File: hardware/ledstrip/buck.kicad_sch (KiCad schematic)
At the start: 5 parts, among them U3 TPS62162DSG

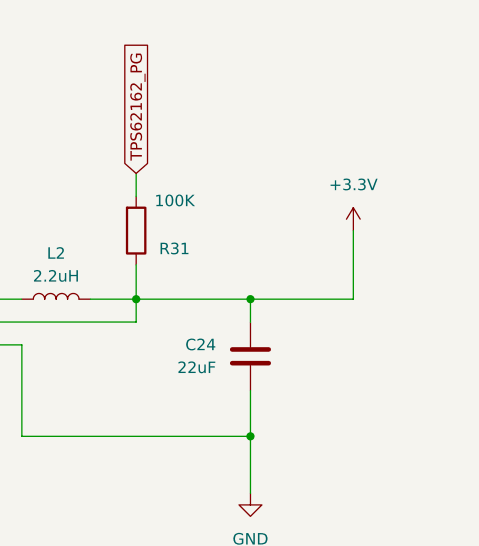
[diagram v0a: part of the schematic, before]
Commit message: Fix ERC errors.
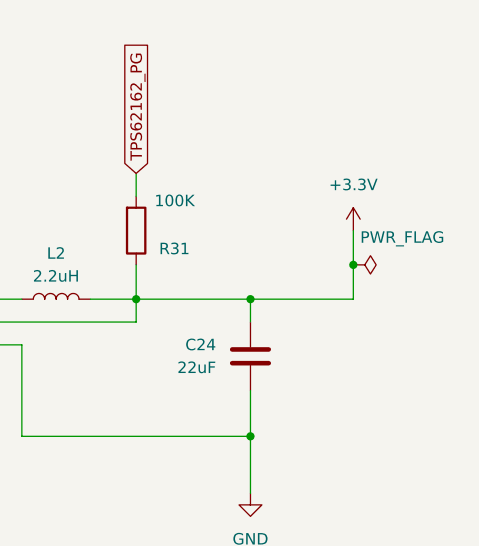
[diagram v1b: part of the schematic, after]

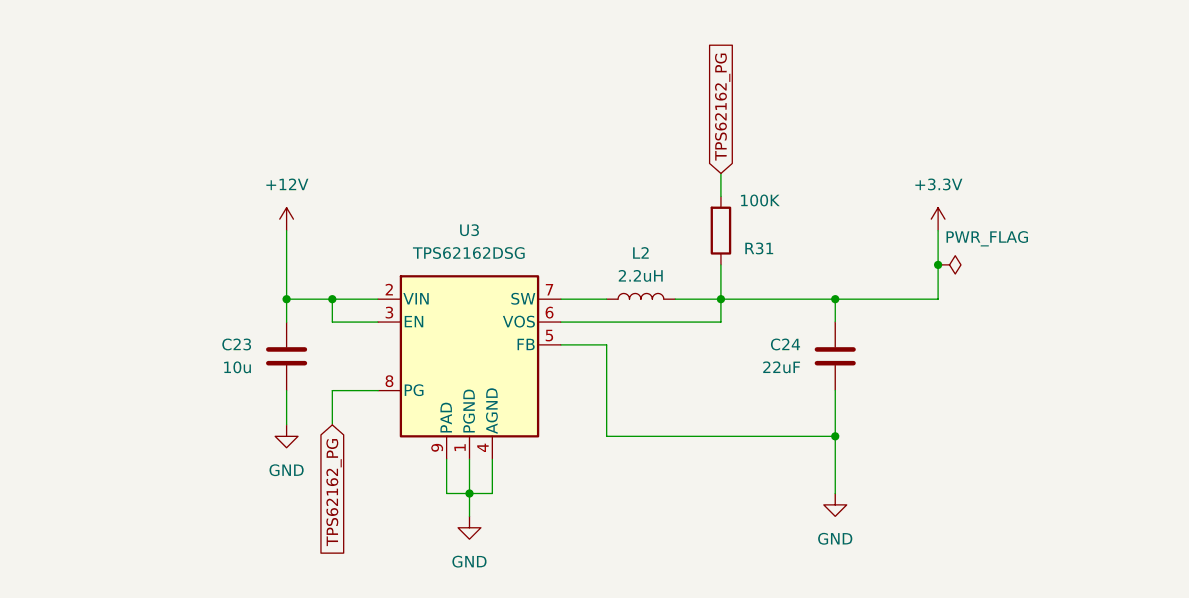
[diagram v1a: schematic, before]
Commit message: Fix last errors in schematics
Missing footprint, missing distributor link.
Updated project sym-lib-table for ERC checks.
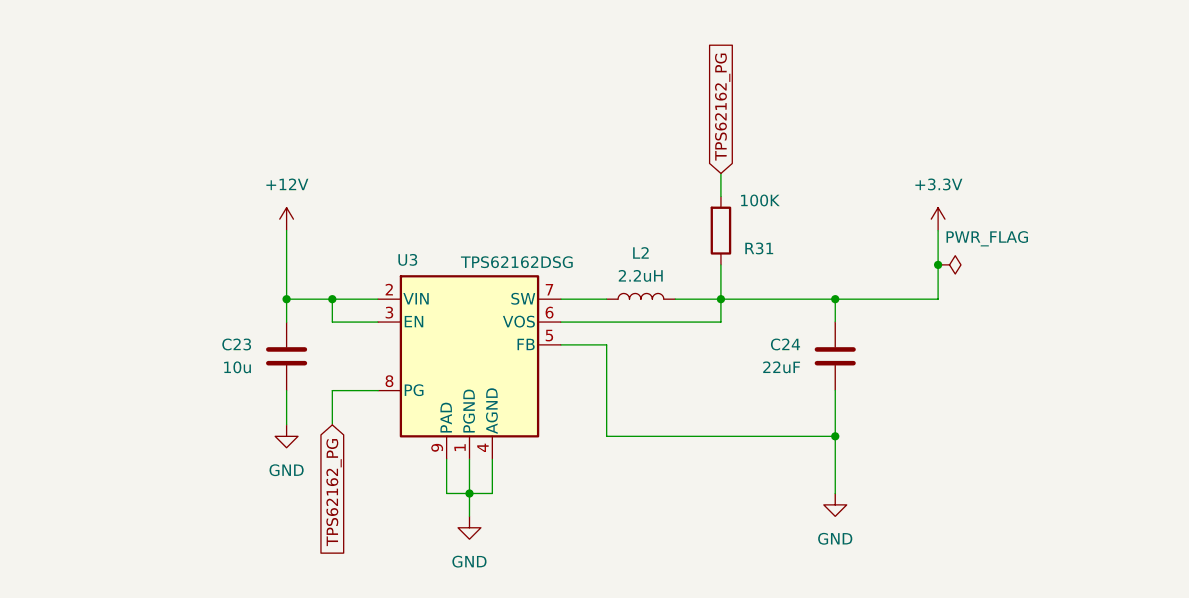
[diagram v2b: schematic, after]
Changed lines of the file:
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@@
 		(on_board yes)
 		(dnp no)
-		(fields_autoplaced yes)
 		(property "Reference" "U3"
-			(at 132.08 71.12 0)
+			(at 125.222 74.422 0)
 			(effects
 				(font
@@
 		)
 		(property "Value" "TPS62162DSG"
-			(at 132.08 73.66 0)
+			(at 137.414 74.676 0)
 			(effects
 				(font

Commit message: Add label on nodes.
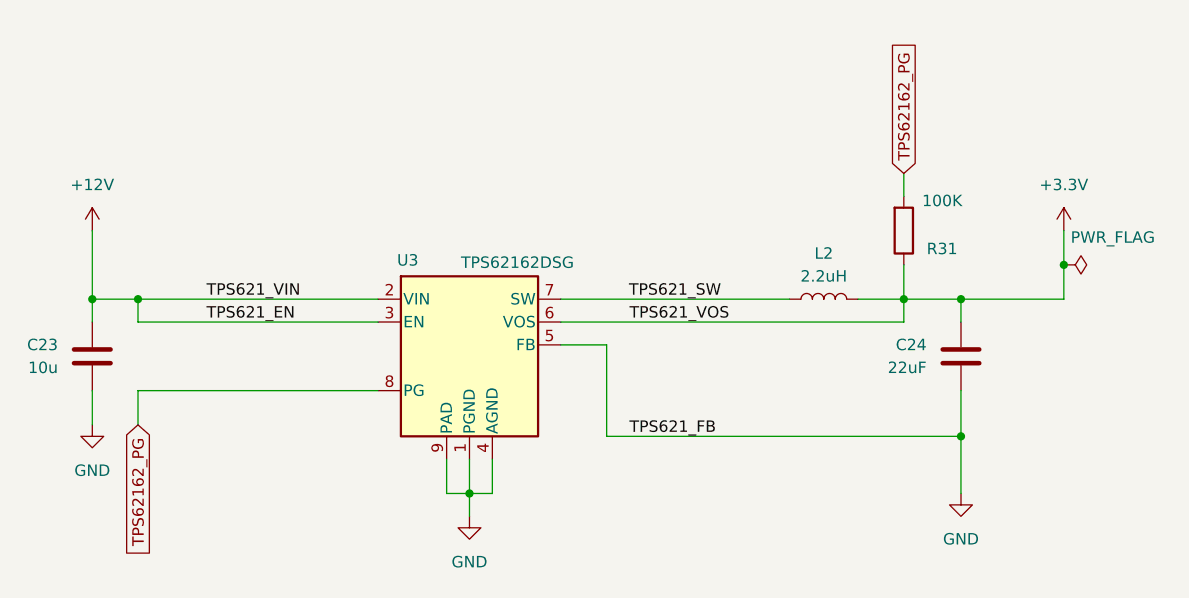
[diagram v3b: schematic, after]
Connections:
- net TPS621_SW: now reaches L2.1, U3.7 (SW)
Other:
- moved on the sheet: C23, C24, L2, R31

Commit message: Fix ERC warnings.
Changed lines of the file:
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@@
-		)
-	)
-	(label "TPS621_VIN"
-		(at 102.87 78.74 0)
-		(effects
-			(font
-				(size 1.27 1.27)
-			)
-			(justify left bottom)
-		)
-	)
-	(label "TPS621_VOS"
-		(at 149.86 81.28 0)
-		(effects
-			(font
-				(size 1.27 1.27)
-			)
-			(justify left bottom)
 		)
 	)
@@
 		(effects
 			(font
-				(size 1.27 1.27)
-			)
-			(justify left bottom)
-		)
-	)
-	(label "TPS621_FB"
-		(at 149.86 93.98 0)
-		(effects
-			(font
-				(size 1.27 1.27)
-			)
-			(justify left bottom)
-		)
-	)
-	(label "TPS621_EN"
-		(at 102.87 81.28 0)
-		(effects
-			(font

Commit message: Minor fixes
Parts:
- C23, C24: MPN (none) -> CL21A106KAYNNN; Manufacturer Part Number CL21A106KAYNNN -> (none)
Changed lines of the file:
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@@
 			)
 		)
-		(property "Manufacturer Part Number" "CL21A106KAYNNN"
+		(property "MPN" "CL21A106KAYNNN"
 			(at 186.69 85.09 0)
 			(effects
@@
 		)
 		(property "Distributor Link 2" "https://www.digikey.fr/fr/products/detail/samsung-electro-mechanics/CL10A226MQ8NRNC/3886851?srsltid=AfmBOopkT6AFjlXVjJGYlzyBS9Mt43m1P9-6SG41ry0KTU876ZZObNuC"
-			(at 186.69 85.09 0)
-			(effects
-				(font
-					(size 1.27 1.27)
-				)
-				(hide yes)
-			)
-		)
-		(property "Disributor Link 1" ""
-			(at 186.69 85.09 0)
-			(effects
-				(font
-					(size 1.27 1.27)
-				)
-				(hide yes)
-			)
-		)
-		(property "Ditributor Link 1" ""
 			(at 186.69 85.09 0)
 			(effects
@@
 			)
 		)
-		(property "Manufacturer Part Number" "CL21A106KAYNNN"
+		(property "MPN" "CL21A106KAYNNN"
 			(at 90.17 85.09 0)
 			(effects
@@
 			)
 		)
-		(property "Disributor Link 1" ""
-			(at 90.17 85.09 0)
-			(effects
-				(font
-					(size 1.27 1.27)
-				)
-				(hide yes)
-			)
-		)
-		(property "Ditributor Link 1" ""
-			(at 90.17 85.09 0)
-			(effects
-				(font
-					(size 1.27 1.27)
-				)
-				(hide yes)
-			)
-		)
 		(pin "1"
 		)
@@
 		)
 		(property "Distributor Link 1" "https://www.mouser.fr/ProductDetail/Texas-Instruments/TPS62162DSGT?qs=gXEV9p%2FxLgc%252BlgWUUl7N3w%3D%3D"
-			(at 132.08 86.36 0)
-			(effects
-				(font
-					(size 1.27 1.27)
-				)
-				(hide yes)
-			)
-		)
-		(property "Disributor Link 1" ""
-			(at 132.08 86.36 0)
-			(effects
-				(font
-					(size 1.27 1.27)
-				)
-				(hide yes)
-			)
-		)
-		(property "Ditributor Link 1" ""
 			(at 132.08 86.36 0)
 			(effects
@@
 			)
 		)
-		(property "Disributor Link 1" ""
-			(at 171.45 78.74 90)
-			(effects
-				(font
-					(size 1.27 1.27)
-				)
-				(hide yes)
-			)
-		)
-		(property "Ditributor Link 1" ""
-			(at 171.45 78.74 90)
-			(effects
-				(font
-					(size 1.27 1.27)
-				)
-				(hide yes)
-			)
-		)
 		(pin "1"
 		)
@@
 			(at 180.34 71.12 0)
 			(effects
-				(font
-					(size 1.27 1.27)
-				)
-				(hide yes)
-			)
-		)
-		(property "Disributor Link 1" ""
-			(at 180.34 71.12 0)
-			(effects
-				(font
-					(size 1.27 1.27)
-				)
-				(hide yes)
-			)
-		)
-		(property "Ditributor Link 1" ""
-			(at 180.34 71.12 0)
-			(effects

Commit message: Update schematics symbols fields for manufactrurer
Update BOM fields.
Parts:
- L2: MPN (none) -> PFL3215-222MEC; Manufacturer (none) -> Coilcraft
- R31: MPN (none) -> RT0805BRB07100KL; Manufacturer (none) -> YAGEO
- U3: MPN (none) -> TPS62162DSGT; Manufacturer (none) -> Texas Instruments
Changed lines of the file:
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@@
+			)
+		)
+		(property "Disributor Link 1" ""
+			(at 186.69 85.09 0)
+			(effects
+				(font
+					(size 1.27 1.27)
+				)
+				(hide yes)
+			)
+		)
+		(property "Ditributor Link 1" ""
+			(at 186.69 85.09 0)
+			(effects
+				(font
+					(size 1.27 1.27)
+				)
+				(hide yes)
+			)
+		)
+		(property "Manufacturer Part Number" ""
+			(at 186.69 85.09 0)
+			(effects
+				(font
+					(size 1.27 1.27)
+				)
+				(hide yes)
 			)
 		)
@@
 			)
 		)
+		(property "Disributor Link 1" ""
+			(at 90.17 85.09 0)
+			(effects
+				(font
+					(size 1.27 1.27)
+				)
+				(hide yes)
+			)
+		)
+		(property "Ditributor Link 1" ""
+			(at 90.17 85.09 0)
+			(effects
+				(font
+					(size 1.27 1.27)
+				)
+				(hide yes)
+			)
+		)
+		(property "Manufacturer Part Number" ""
+			(at 90.17 85.09 0)
+			(effects
+				(font
+					(size 1.27 1.27)
+				)
+				(hide yes)
+			)
+		)
 		(pin "1"
 		)
@@
 		)
 		(property "Distributor Link 1" "https://www.mouser.fr/ProductDetail/Texas-Instruments/TPS62162DSGT?qs=gXEV9p%2FxLgc%252BlgWUUl7N3w%3D%3D"
+			(at 132.08 86.36 0)
+			(effects
+				(font
+					(size 1.27 1.27)
+				)
+				(hide yes)
+			)
+		)
+		(property "Manufacturer" "Texas Instruments"
+			(at 132.08 86.36 0)
+			(effects
+				(font
+					(size 1.27 1.27)
+				)
+				(hide yes)
+			)
+		)
+		(property "MPN" "TPS62162DSGT"
+			(at 132.08 86.36 0)
+			(effects
+				(font
+					(size 1.27 1.27)
+				)
+				(hide yes)
+			)
+		)
+		(property "Disributor Link 1" ""
+			(at 132.08 86.36 0)
+			(effects
+				(font
+					(size 1.27 1.27)
+				)
+				(hide yes)
+			)
+		)
+		(property "Ditributor Link 1" ""
+			(at 132.08 86.36 0)
+			(effects
+				(font
+					(size 1.27 1.27)
+				)
+				(hide yes)
+			)
+		)
+		(property "Manufacturer Part Number" ""
 			(at 132.08 86.36 0)
 			(effects
@@
 			)
 		)
+		(property "Manufacturer" "Coilcraft"
+			(at 171.45 78.74 90)
+			(effects
+				(font
+					(size 1.27 1.27)
+				)
+				(hide yes)
+			)
+		)
+		(property "MPN" "PFL3215-222MEC"
+			(at 171.45 78.74 90)
+			(effects
+				(font
+					(size 1.27 1.27)
+				)
+				(hide yes)
+			)
+		)
 		(property "Distributor Link 2" "https://www.coilcraft.com/en-us/products/power/shielded-inductors/molded-inductor/pfl/pfl3215/pfl3215-222/?srsltid=AfmBOooloSXEMlP32bATBb0fG8MwtySnY4A9GXMUtQt98iXKMXBtuEx7"
+			(at 171.45 78.74 90)
+			(effects
+				(font
+					(size 1.27 1.27)
+				)
+				(hide yes)
+			)
+		)
+		(property "Disributor Link 1" ""
+			(at 171.45 78.74 90)
+			(effects
+				(font
+					(size 1.27 1.27)
+				)
+				(hide yes)
+			)
+		)
+		(property "Ditributor Link 1" ""
+			(at 171.45 78.74 90)
+			(effects
+				(font
+					(size 1.27 1.27)
+				)
+				(hide yes)
+			)
+		)
+		(property "Manufacturer Part Number" ""
 			(at 171.45 78.74 90)
 			(effects
@@
 			)
 		)
+		(property "Manufacturer" "YAGEO"
+			(at 180.34 71.12 0)
+			(effects
+				(font
+					(size 1.27 1.27)
+				)
+				(hide yes)
+			)
+		)
+		(property "MPN" "RT0805BRB07100KL"
+			(at 180.34 71.12 0)
+			(effects
+				(font
+					(size 1.27 1.27)
+				)
+				(hide yes)
+			)
+		)
 		(property "Distributor Link 2" "https://www.digikey.com/en/products/detail/yageo/RT0805BRB07100KL/5931185"
 			(at 180.34 71.12 0)
 			(effects
+				(font
+					(size 1.27 1.27)
+				)
+				(hide yes)
+			)
+		)
+		(property "Disributor Link 1" ""
+			(at 180.34 71.12 0)
+			(effects
+				(font
+					(size 1.27 1.27)
+				)
+				(hide yes)
+			)
+		)
+		(property "Ditributor Link 1" ""
+			(at 180.34 71.12 0)
+			(effects
+				(font
+					(size 1.27 1.27)
+				)
+				(hide yes)
+			)
+		)
+		(property "Manufacturer Part Number" ""
+			(at 180.34 71.12 0)
+			(effects
